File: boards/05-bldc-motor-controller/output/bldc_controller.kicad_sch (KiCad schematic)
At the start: 51 parts, among them J1 Power Input, J2 Motor Output, J3 Hall Sensors, J4 SWD-6, Q1 IRLZ44N, Q2 IRLZ44N, Q3 IRLZ44N, Q4 IRLZ44N, Q5 IRLZ44N, Q6 IRLZ44N, U1 LM2596-5.0, U10 STM32G431K8Tx, U2 AMS1117-3.3, U3 DRV8301, Y1 8MHz

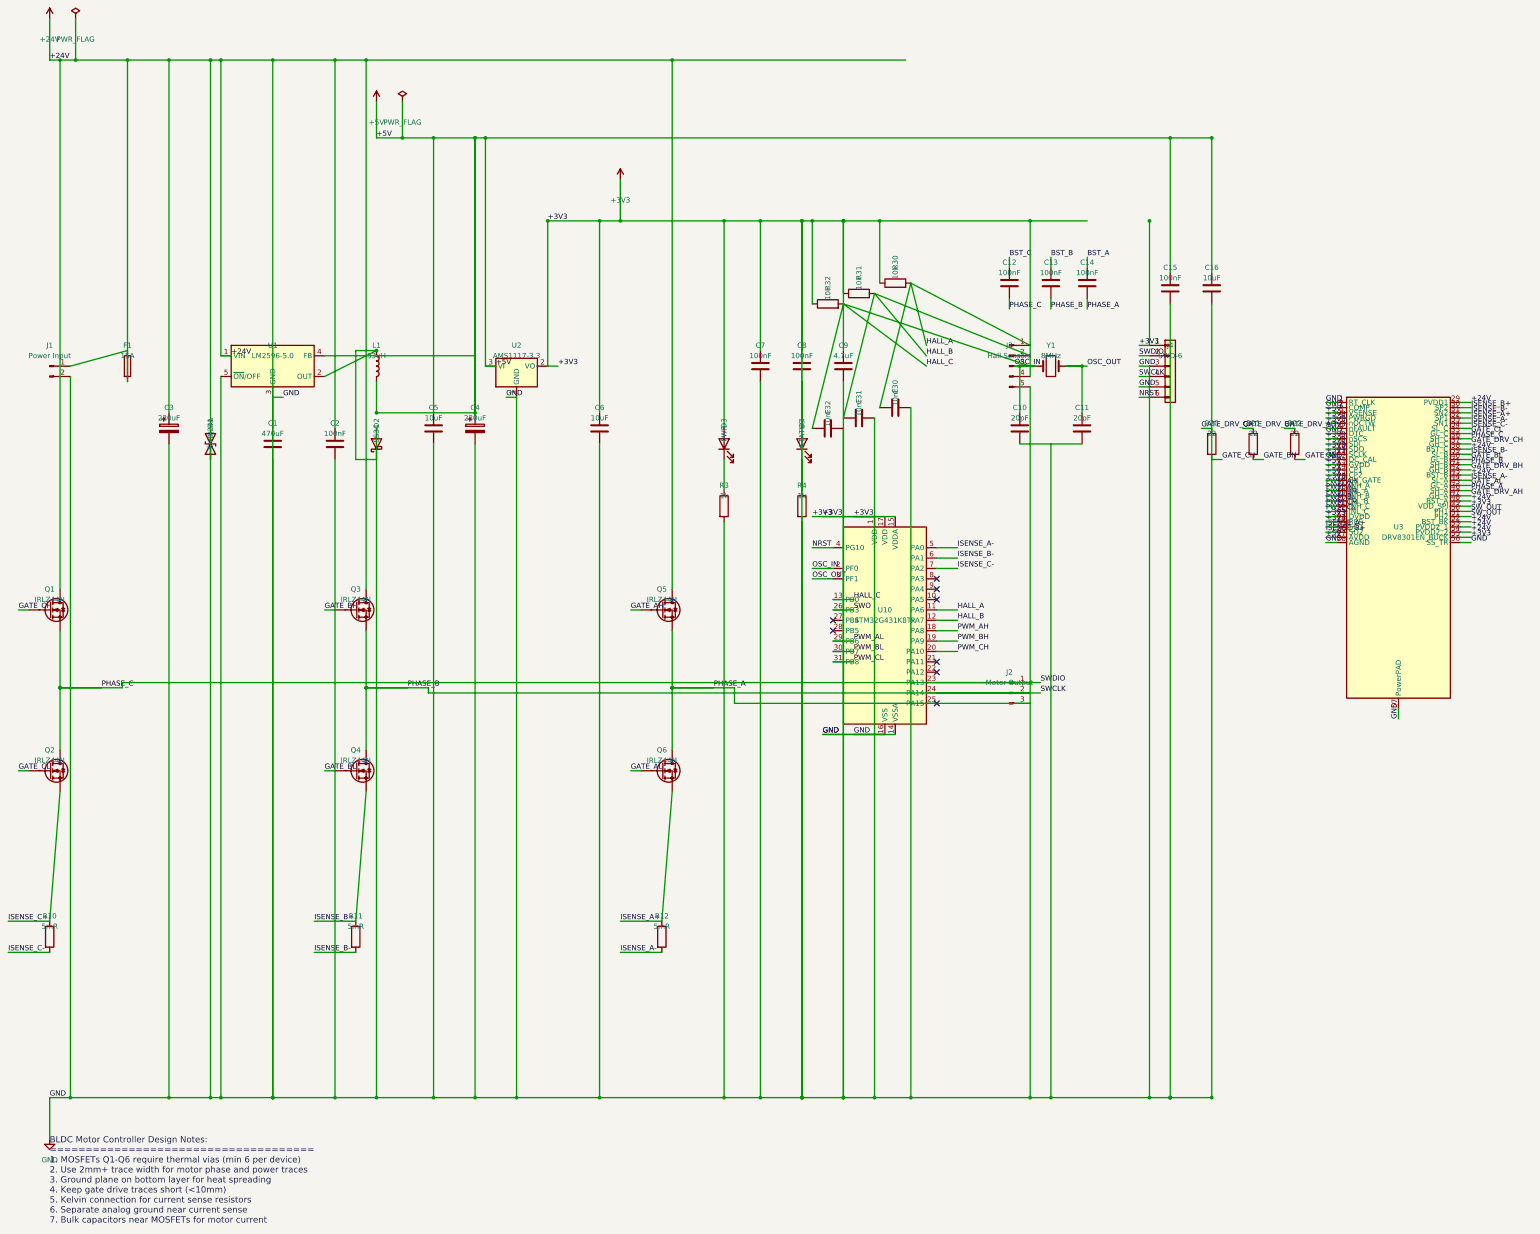
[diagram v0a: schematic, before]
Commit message: fix(boards/05): schematic-emit defects — LED polarity, BST chain, NCs, J4/U2/U1 pin maps, fuse nets (closes #3397)
Eliminates all 36 residual sync-netlist mismatches on board 05
(re-measured at 36 on current main; now 0 on both the unrouted and
routed committed artifacts). Per-defect triage:

1. LED polarity (D1/D3/D4) — REAL, PCB-side. generate_led_0805 mapped
   the anode to pad 1 (the LED_0805 footprint's cathode pad), and the
   PCB put the resistor on the anode side while the schematic
   LEDIndicator puts it on the cathode side; D1 (TVS) had its
   generate_diode_sma (net_a, net_k) args swapped, installing it
   backwards. Fixed the generator pad map and call sites; schematic
   gains PWR_LED/STATUS_LED labels (collision-aware stubs) so net
   names match the PCB.
2. Bootstrap chain (U3 BST pins) — REAL, both sides. U3.38/43/48 and
   cap C12-C14 high sides were DC-tied to +24V, defeating the
   bootstrap supply; the schematic's BootstrapCapacitorArray BST_x
   nets floated. Both sides now use BST_C/B/A nets (pin-to-cap-to-
   phase). Pins 29/53/54 (PVDD) stay +24V correctly; pin 52 (BST_BK)
   left as documented DC tie — no buck bootstrap cap exists on the
   board and it was not part of the 36.
3. U10 unused-pin NCs — REAL, PCB-side. Pads 8/9/10/21/22/25/27/28
   were tied to GND "for the autorouter" while the schematic marks
   them no-connect; pads now carry per-pad unconnected-(U10-...) nets
   matching KiCad's netlist-export convention.
4. J4 SWD pinout — REAL, schematic-side. Schematic emitted generic
   SWD-6 (GND/SWCLK/GND/NRST on pins 3-6, no SWO); now matches the
   PCB pad map (SWCLK/SWO/NRST/GND), restoring the MCU SWO trace pin.
   DebugHeader.connect_to_rails dropped (it would wire pin 3 — now
   SWCLK — onto the GND rail). J4 PCB position untouched (#3424).
5. U2 LDO pin swap — REAL, PCB-side. SOT-223 pads used 78xx-style
   (VIN/GND/VOUT); AMS1117 is GND/VOUT/VIN. Schematic was correct.
6. U1 buck pin swap — REAL, PCB-side. TO-263-5 pads 2/3/4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
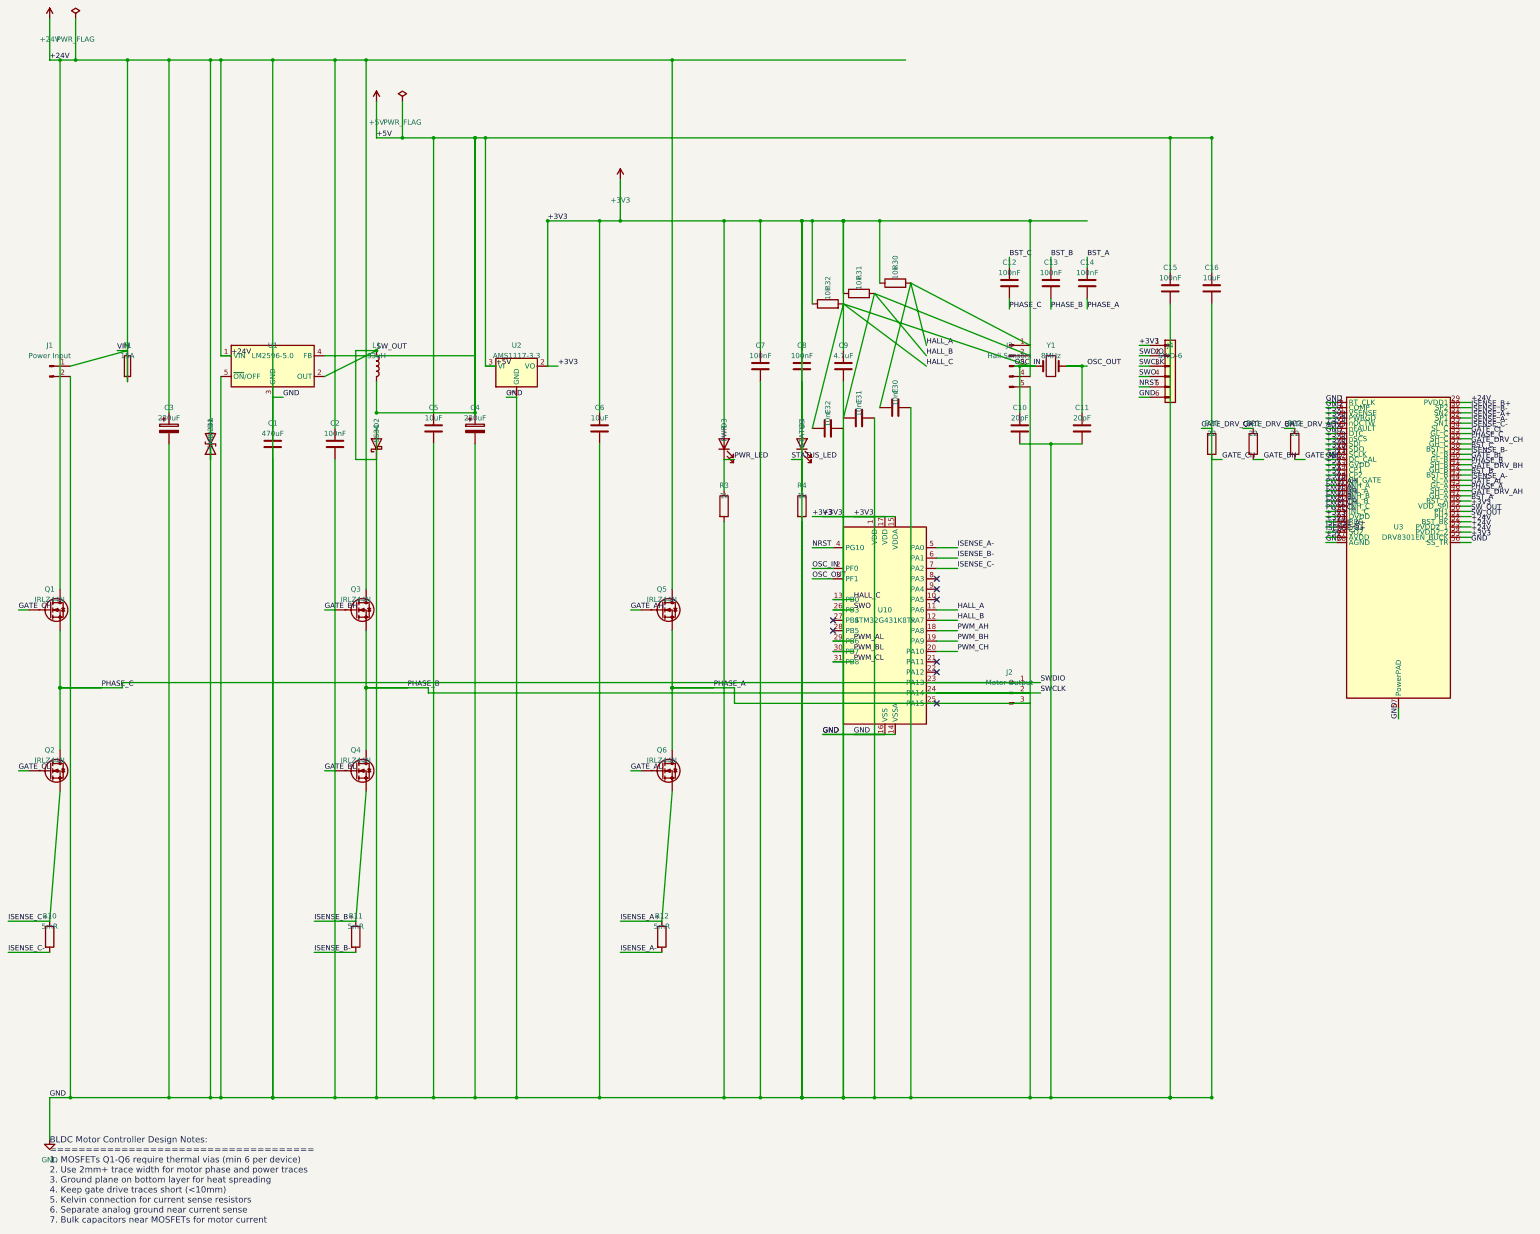
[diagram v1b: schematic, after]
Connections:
- net +24V: now also C10.2, C11.2, J4.6 (Pin_6); no longer J4.3 (Pin_3), J4.5 (Pin_5), U3.38 (BST_C), U3.43 (BST_B), U3.48 (BST_A)
- net BST_A: now also U3.48 (BST_A)
- net BST_B: now also U3.43 (BST_B)
- net BST_C: now also U3.38 (BST_C)
- net NRST: now also J4.5 (Pin_5); no longer J4.6 (Pin_6)
- net PHASE_B: now also J4.3 (Pin_3); no longer J4.4 (Pin_4)
- net SWO: now also J4.4 (Pin_4)
- net SW_OUT: now also D2.1 (K), L1.1, U1.2 (OUT)
- net VIN: now reaches F1.1, J1.1 (Pin_1)
- net PWR_LED: now reaches D3.1 (K), R3.1

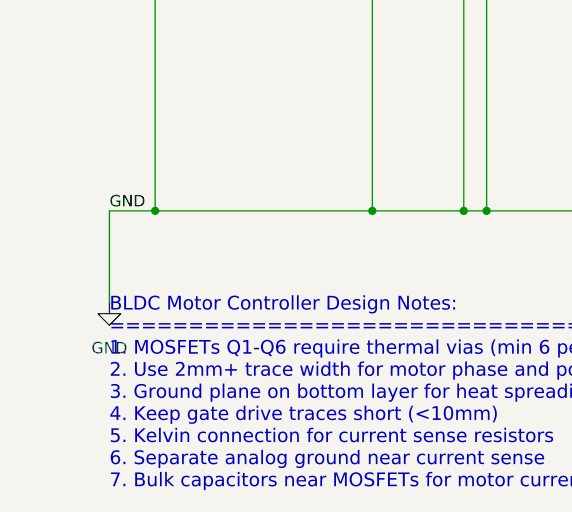
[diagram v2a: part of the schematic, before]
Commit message: fix(board-05): add GND PWR_FLAG to clear power_pin_not_driven ERC error (#3831)
The BLDC controller schematic placed PWR_FLAG symbols on the +24V and
+5V rails but omitted one on GND, on the incorrect assumption (stale
comment) that AMS1117.GND drives the GND net. AMS1117.GND is a
power_input pin (only VO is power_output), so no power_output source
drove GND and every GND power_input pin (U1 Pin 3 [GND] included) fired
the blocking power_pin_not_driven ERC error on every clean build under
both kct erc and native kicad-cli sch erc.

Add a PWR_FLAG on the GND rail mirroring the +24V/+5V pattern (placed
7mm east of the GND symbol, wired up from RAIL_GND+10 to RAIL_GND with a
junction), correct the stale comment, regenerate the committed
schematic, and add regression guards for the power_pin_not_driven error
and the GND PWR_FLAG's presence.

Closes #3827

Co-authored-by: Claude Opus 4.8 <noreply@anthropic.com>
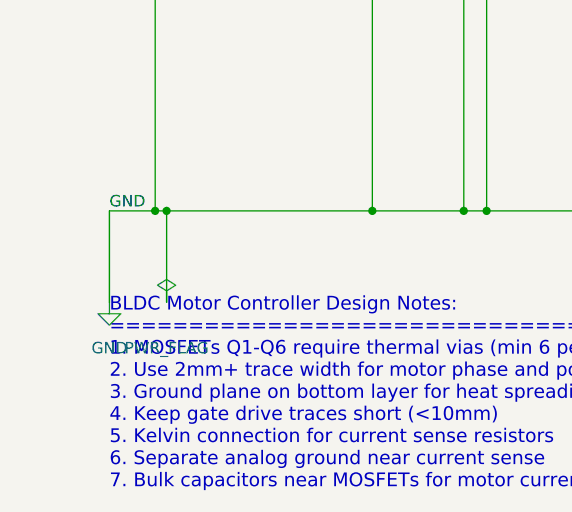
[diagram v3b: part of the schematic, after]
